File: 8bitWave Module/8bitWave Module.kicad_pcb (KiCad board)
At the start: 2 copper layers, 99.7 x 64.1 mm, 48 parts, among them IC1 0.96_I2C_OLED, IC2 0.91_I2C_OLED, J1 REM, J2 EAR, J3 EXTENSION, M1 Mounting, M2 Mounting, M3 Mounting, M4 Mounting, SW1 UP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

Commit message: Faceplate sketched out
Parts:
- added REF**: logo, icons:logo, F.Cu at (86.4, 103.1)
- moved J3 5.72 mm to (168.3, 95.2)
- moved JP5 5.72 mm to (168.3, 113.0)
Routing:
- net +5V: track 105.4 -> 111.1 mm
- net +3V3: track 45.0 -> 50.7 mm
- net /D2: track 16.4 -> 10.7 mm
- net /D4: track 13.9 -> 8.41 mm
- net /D8: track 6.99 -> 12.0 mm
- net /SCL: track 115.2 -> 119.8 mm
- net /SDA: track 117.7 -> 121.9 mm
- net Net-(IC1-Pad2): track 113.0 -> 112.2 mm
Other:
- board text removed: "8bit Wave"

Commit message: Finishing touches
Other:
- board text added: "AUDIO AMPLIFIER"
- board text added: "Arduino Nano"
- board text added: "BYPASS"
- board text added: "EXTENSION"
- board text added: "GAIN"
- board text added: "I2C PULL-UP (INSTALL IF NEEDED)"
- board text added: "NO_FILTER"
- board text removed: "I2C PULL-UP"
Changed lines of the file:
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@@
     (area 66.04 72.39 172.720001 147.955001)
     (thickness 1.6)
-    (drawings 54)
+    (drawings 60)
     (tracks 481)
     (zones 0)
@@
       (rotate (xyz 0 0 0))
     )
-  )
-  (module i2c_oled:0.91_I2C_OLED (layer F.Cu)
-    (at 102.235 104.775)
-    (fp_text reference IC2 (at 1.905 -0.127 90) (layer F.SilkS)
-      (effects (font (size 1 1) (thickness 0.15)))
-    )
-    (fp_text value 0.91_I2C_OLED (at 15.24 0) (layer F.Fab)
-      (effects (font (size 1 1) (thickness 0.15)))
-    )
-    (fp_line (start 3 3.81) (end 33 3.81) (layer Dwgs.User) (width 0.15))
-    (fp_line (start 33 3.81) (end 33 -3.81) (layer Dwgs.User) (width 0.15))
-    (fp_line (start 33 -3.81) (end 3 -3.81) (layer Dwgs.User) (width 0.15))
-    (fp_line (start 3 0) (end 3 3.81) (layer Dwgs.User) (width 0.15))
-    (fp_line (start 3 0) (end 3 -3.81) (layer Dwgs.User) (width 0.15))
-    (fp_line (start -1.27 6) (end 36.7 6) (layer F.Fab) (width 0.15))
-    (fp_line (start 36.7 6) (end 36.7 -6) (layer F.Fab) (width 0.15))
-    (fp_line (start 36.7 -6) (end -1.27 -6) (layer F.Fab) (width 0.15))
-    (fp_line (start -1.3 0) (end -1.3 6) (layer F.Fab) (width 0.15))
-    (fp_line (start -1.3 0) (end -1.3 -6) (layer F.Fab) (width 0.15))
-    (pad 1 thru_hole rect (at 0 3.81) (size 1.524 1.524) (drill 0.762) (layers *.Cu *.Mask)
-      (net 6 GND))
-    (pad 2 thru_hole circle (at 0 1.27) (size 1.524 1.524) (drill 0.762) (layers *.Cu *.Mask)
-      (net 38 "Net-(IC1-Pad2)"))
-    (pad 3 thru_hole circle (at 0 -1.27) (size 1.524 1.524) (drill 0.762) (layers *.Cu *.Mask)
-      (net 9 /SCL))
-    (pad 4 thru_hole circle (at 0 -3.81) (size 1.524 1.524) (drill 0.762) (layers *.Cu *.Mask)
-      (net 8 /SDA))
   )
   (module Capacitors_THT:C_Disc_D4.7mm_W2.5mm_P5.00mm (layer F.Cu)
@@
       (effects (font (size 1 1) (thickness 0.15)))
     )
-    (fp_text value USER (at -1.905 0.635 360) (layer F.SilkS)
+    (fp_text value USER (at -1.905 0 360) (layer F.SilkS)
       (effects (font (size 0.8 0.8) (thickness 0.1)))
     )
@@
     )
   )
+  (module i2c_oled:0.91_I2C_OLED (layer F.Cu)
+    (at 102.235 104.775)
+    (fp_text reference IC2 (at 1.905 -0.127 90) (layer F.SilkS)
+      (effects (font (size 1 1) (thickness 0.15)))
+    )
+    (fp_text value 0.91_I2C_OLED (at 15.24 0) (layer F.SilkS)
+      (effects (font (size 1 1) (thickness 0.15)))
+    )
+    (fp_line (start 3 3.81) (end 33 3.81) (layer Dwgs.User) (width 0.15))
+    (fp_line (start 33 3.81) (end 33 -3.81) (layer Dwgs.User) (width 0.15))
+    (fp_line (start 33 -3.81) (end 3 -3.81) (layer Dwgs.User) (width 0.15))
+    (fp_line (start 3 0) (end 3 3.81) (layer Dwgs.User) (width 0.15))
+    (fp_line (start 3 0) (end 3 -3.81) (layer Dwgs.User) (width 0.15))
+    (fp_line (start -1.27 6) (end 36.7 6) (layer F.SilkS) (width 0.15))
+    (fp_line (start 36.7 6) (end 36.7 -6) (layer F.SilkS) (width 0.15))
+    (fp_line (start 36.7 -6) (end -1.27 -6) (layer F.SilkS) (width 0.15))
+    (fp_line (start -1.3 0) (end -1.3 6) (layer F.SilkS) (width 0.15))
+    (fp_line (start -1.3 0) (end -1.3 -6) (layer F.SilkS) (width 0.15))
+    (pad 1 thru_hole rect (at 0 3.81) (size 1.524 1.524) (drill 0.762) (layers *.Cu *.Mask)
+      (net 6 GND))
+    (pad 2 thru_hole circle (at 0 1.27) (size 1.524 1.524) (drill 0.762) (layers *.Cu *.Mask)
+      (net 38 "Net-(IC1-Pad2)"))
+    (pad 3 thru_hole circle (at 0 -1.27) (size 1.524 1.524) (drill 0.762) (layers *.Cu *.Mask)
+      (net 9 /SCL))
+    (pad 4 thru_hole circle (at 0 -3.81) (size 1.524 1.524) (drill 0.762) (layers *.Cu *.Mask)
+      (net 8 /SDA))
+  )
+  (gr_text "Arduino Nano" (at 153.67 99.695) (layer B.SilkS)
+    (effects (font (size 0.8 0.8) (thickness 0.1)) (justify mirror))
+  )
+  (gr_text "AUDIO\nAMPLIFIER" (at 104.14 89.535) (layer B.SilkS)
+    (effects (font (size 0.8 0.8) (thickness 0.1)) (justify mirror))
+  )
+  (gr_text EXTENSION (at 165.735 102.87 90) (layer B.SilkS)
+    (effects (font (size 0.8 0.8) (thickness 0.1)) (justify mirror))
+  )
+  (gr_text BYPASS (at 113.665 87.63) (layer B.SilkS)
+    (effects (font (size 0.8 0.8) (thickness 0.1)) (justify mirror))
+  )
+  (gr_text NO_FILTER (at 113.665 82.55) (layer B.SilkS)
+    (effects (font (size 0.8 0.8) (thickness 0.1)) (justify mirror))
+  )
+  (gr_text GAIN (at 106.68 82.55) (layer B.SilkS)
+    (effects (font (size 0.8 0.8) (thickness 0.1)) (justify mirror))
+  )
   (gr_text github.com/tebl (at 84.328 107.696) (layer F.SilkS)
     (effects (font (size 1 1) (thickness 0.1)))
@@
     (effects (font (size 0.8 0.8) (thickness 0.1)) (justify left mirror))
   )
-  (gr_text "I2C\nPULL-UP" (at 147.32 128.27) (layer B.SilkS)
+  (gr_text "I2C\nPULL-UP\n\n(INSTALL IF\nNEEDED)" (at 147.32 128.27) (layer B.SilkS)
     (effects (font (size 0.8 0.8) (thickness 0.1)) (justify mirror))
   )

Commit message: PAM8403
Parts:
- removed IC2: 0.91_I2C_OLED, i2c_oled:0.91_I2C_OLED
- removed JP2: NO_FILTER, Pin_Headers:Pin_Header_Straight_1x02_Pitch2.54mm
- removed JP3: AMPLIFY, Pin_Headers:Pin_Header_Straight_1x03_Pitch2.54mm
- removed RV1: 10k, Potentiometers:Potentiometer_Triwood_RM-065
- added A3: GF1002, gf1002:GF1002_reverse, F.Cu at (97.2, 110.5)
- added D3: 1n4001, Diodes_THT:D_DO-41_SOD81_P10.16mm_Horizontal, F.Cu at (148.0, 131.4)
- added J4: DC IN, Connectors:BARREL_JACK, F.Cu at (156.8, 128.9)
- added J5: LP_FILTER, Pin_Headers:Pin_Header_Straight_2x03_Pitch2.54mm, F.Cu at (134.0, 104.1)
- added J6: SPI, Pin_Headers:Pin_Header_Straight_1x03_Pitch2.54mm, F.Cu at (72.4, 95.2)
- added J7: EAR_SEL, Pin_Headers:Pin_Header_Straight_2x06_Pitch2.54mm, F.Cu at (115.6, 104.1)
- added JP6: PWR_SEL, Pin_Headers:Pin_Header_Straight_1x03_Pitch2.54mm, F.Cu at (151.8, 131.4)
- added REF**: logo, icons:logo, F.Cu at (84.5, 96.9)
- added RV2: 10k, pot_vertical:Potentiometer_Trimmer_Bourns_3296W, F.Cu at (123.8, 88.9)
- C10: value 100uF -> 220uF
- C9: value 10pF -> 47nF
- JP1: footprint Pin_Headers:Pin_Header_Straight_1x02_Pitch2.54mm -> Pin_Headers:Pin_Header_Straight_1x03_Pitch2.54mm
- R5: value 100 -> 10
- R6, R7: value 220 -> 330
- REF**: moved to B.Cu
- moved R5 51.5 mm to (125.7, 112.4), turned to 180 degrees
- moved C9 32.1 mm to (111.7, 104.8), turned to 180 degrees
- moved R7 28.0 mm to (137.8, 123.8), turned to 0 degrees
- moved R6 27.3 mm to (137.8, 127.6), turned to 0 degrees
- moved R8 22.0 mm to (137.8, 108.6), turned to 270 degrees
- moved REF** 18.5 mm to (88.3, 121.5), turned to 180 degrees
- moved R9 17.8 mm to (141.6, 108.6), turned to 270 degrees
- moved C10 16.5 mm to (102.9, 107.3)
- moved C5 8.70 mm to (111.7, 101.0), turned to 180 degrees
- moved C8 8.64 mm to (102.2, 90.2), turned to 180 degrees
- moved JP4 8.13 mm to (108.6, 80.0), turned to 90 degrees
- moved JP1 6.98 mm to (98.4, 80.0)
- moved U1 6.54 mm to (106.0, 89.5)
- moved C7 5.53 mm to (109.9, 85.7), turned to 90 degrees
- moved C6 5.12 mm to (118.1, 94.6), turned to 270 degrees
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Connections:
- A1 pad 30: (no net) -> VIN
- C5 pad 1: +5V -> VEXT
- C6 pad 1: +5V -> VEXT
- C9 pad 1: Net-(C10-Pad2) -> LM386+
- J2 pad 1: GND -> Net-(J2-Pad1)
- J2 pad 5: Net-(J2-Pad5) -> Net-(C10-Pad2)
- R3 pad 1: /SOUND -> Net-(J5-Pad5)
- U1 pad 5: Net-(C10-Pad1) -> LM386+
- U1 pad 6: +5V -> VEXT
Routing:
- net VEXT: track 0.00 -> 80.7 mm, vias 0 -> 6
- net /SOUND: track 108.0 -> 41.0 mm, vias 1 -> 0
- net AUD_LINE: track 0.00 -> 67.0 mm, vias 0 -> 1
- net Net-(J2-Pad1): track 0.00 -> 64.1 mm, vias 0 -> 2
- net /SDA: track 121.9 -> 58.4 mm, vias 2 -> 1
- net /SCK: track 79.8 -> 142.9 mm, vias 2 -> 3
- net /SCL: track 119.8 -> 61.0 mm, vias 4 -> 1
- net /MOSI: track 90.0 -> 148.7 mm, vias 3 -> 5
- net /MISO: track 90.1 -> 143.9 mm
- net GF1002+: track 0.00 -> 39.6 mm
- net GF1002-: track 0.00 -> 37.6 mm
- net Net-(J5-Pad5): track 0.00 -> 28.0 mm, vias 0 -> 1
- net Net-(C10-Pad2): track 31.2 -> 58.4 mm, vias 0 -> 2
- net Net-(D1-Pad2): track 99.7 -> 72.8 mm, vias 0 -> 1
- net Net-(D2-Pad2): track 13.9 -> 39.6 mm
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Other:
- outline, holes or cut-outs redrawn
- net class Power added: clearance 0.381, trace_width 0.381, via_dia 1, via_drill 0.4
- board text added: "(GF1002 module to be installed as alternative amplifier, mounted upside down - adjust to fit under faceplate)"
- board text added: "(PWR_SEL should be set to intended voltage, mark selection for reference. 9V only with LM386 option.)"
- board text added: "5V (DC)"
- board text added: "9V (DC)"
- board text added: "EAR"
- board text added: "EAR_SEL"
- board text added: "EAR_SEL (J7): 01-02 Direct* 11-12 03-04 Direc (AC) 11-12 05-06 LM386 11-12 07-08 GF1002 09-10"
- board text added: "G"
- board text added: "GND"
- board text added: "L"
- board text added: "LM386"
- board text added: "LM386 VOLUME"
- board text added: "LP_FILTER"
- board text added: "LP_FILTER (J6): 1-2 Disabled* 3-4 Enabled 5-6"
- board text added: "R"
- board text added: "REM"
- board text added: "SCL"
- board text added: "SDA"
- board text added: "VCC"
- board text removed: "1-2 Direct 2-3 Amplified"
- board text removed: "AUDIO AMPLIFIER"
- board text removed: "NO_FILTER"

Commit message: Gerber export
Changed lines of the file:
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@@
     (visible_elements 7FFFFFFF)
     (pcbplotparams
-      (layerselection 0x011fc_80000001)
+      (layerselection 0x011fc_ffffffff)
       (usegerberextensions true)
       (usegerberattributes false)
@@
     (descr "LED, diameter 5.0mm, 2 pins, http://cdn-reichelt.de/documents/datenblatt/A500/LL-504BC2E-009.pdf")
     (tags "LED diameter 5.0mm 2 pins")
-    (fp_text reference D2 (at 1.27 -3.96 270) (layer F.SilkS)
-      (effects (font (size 1 1) (thickness 0.15)))
-    )
+    (fp_text reference D2 (at 1.27 0 270) (layer F.SilkS)
+      (effects (font (size 1 1) (thickness 0.15)))
+    )

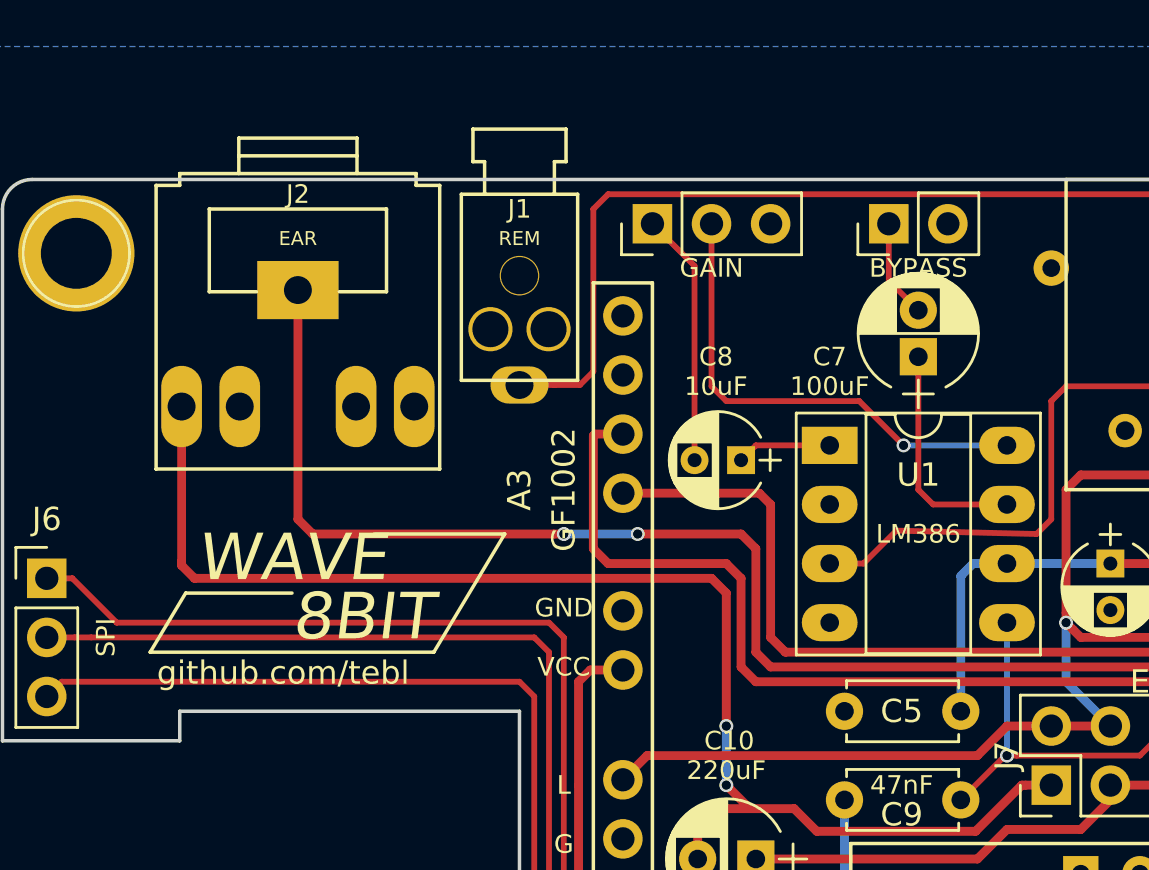
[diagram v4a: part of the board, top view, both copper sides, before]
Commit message: Moved bypass cap, gain jumpers
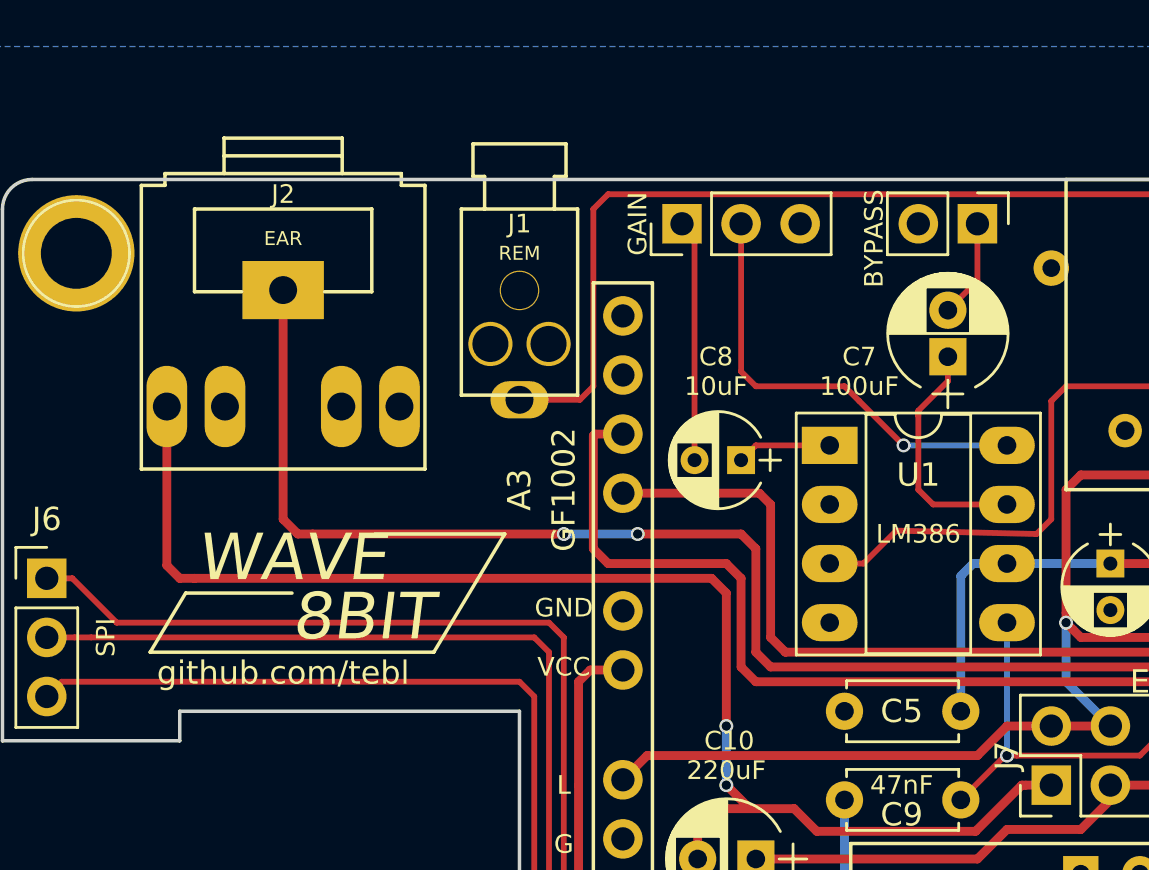
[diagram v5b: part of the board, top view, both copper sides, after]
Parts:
- moved JP4 3.81 mm to (112.4, 80.0), turned to 270 degrees
- moved C7 1.27 mm to (111.1, 85.7)
- moved JP1 1.27 mm to (99.7, 80.0)
- moved J1 0.64 mm to (92.7, 79.4)
- moved J2 0.64 mm to (82.5, 84.5)
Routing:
- net Net-(JP1-Pad2): track 20.7 -> 19.1 mm
- net Net-(J2-Pad1): track 64.1 -> 64.8 mm
- net Net-(C10-Pad2): track 58.4 -> 59.0 mm
- net /REM: track 93.0 -> 93.6 mm
- net Net-(C8-Pad2): track 10.9 -> 10.4 mm
- net Net-(C7-Pad1): track 9.79 -> 10.3 mm

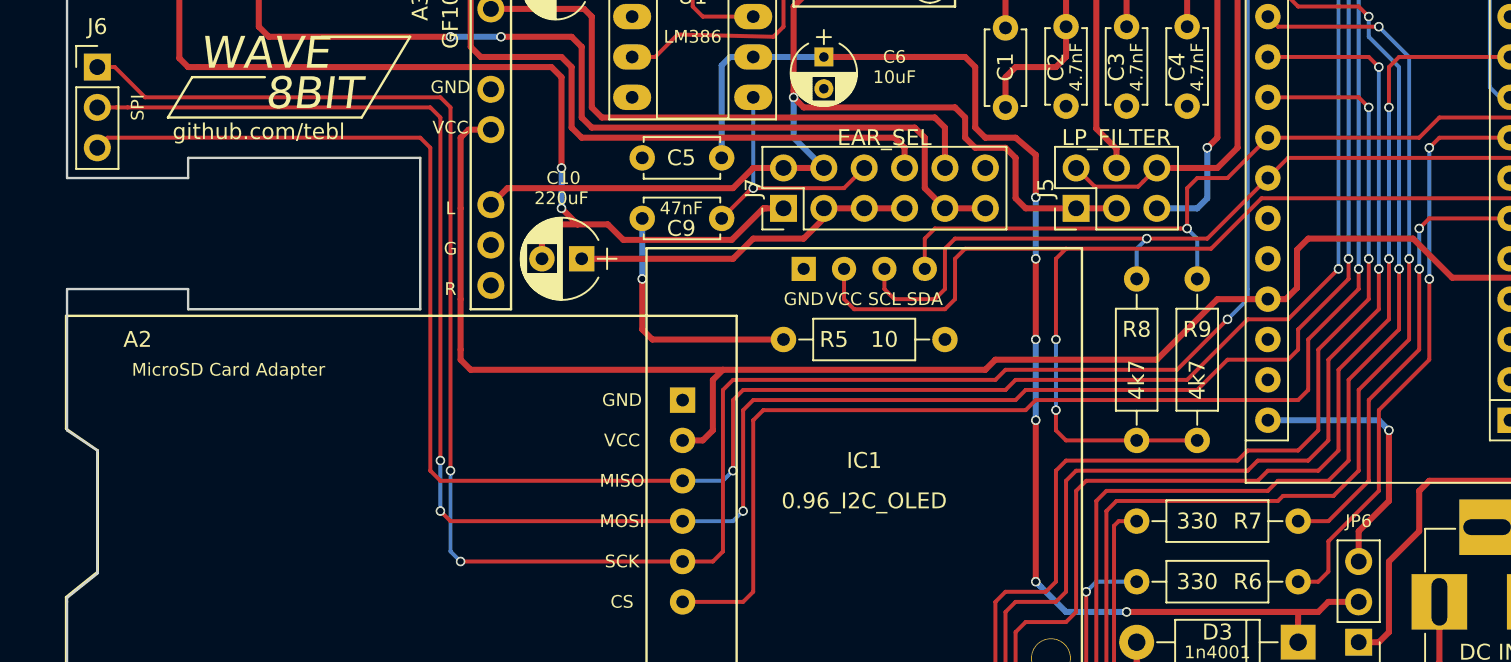
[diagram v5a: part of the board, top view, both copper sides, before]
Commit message: Tweaked module and placement
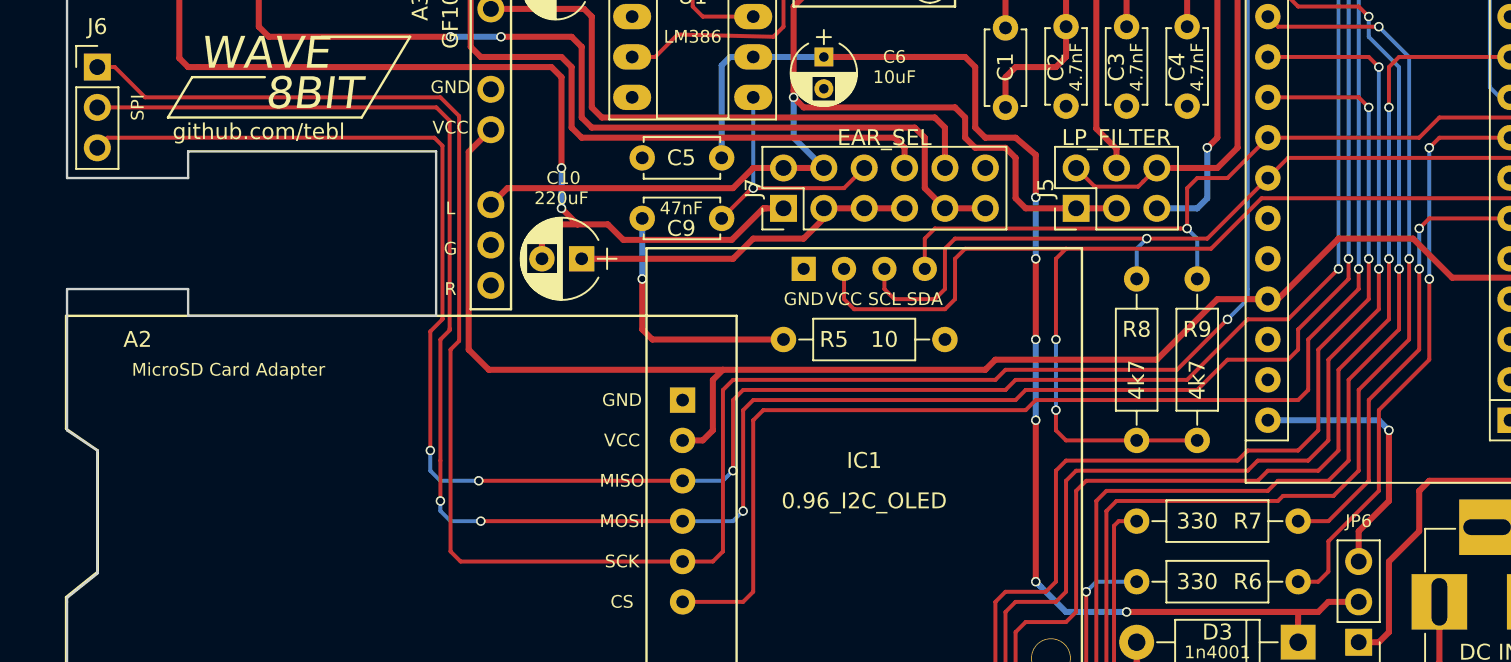
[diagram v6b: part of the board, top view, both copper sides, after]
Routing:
- net +5V: track 133.4 -> 130.1 mm
- net /MISO: track 143.9 -> 145.1 mm, vias 3 -> 5
- net /MOSI: track 148.7 -> 149.3 mm
- net /SCK: track 142.9 -> 143.4 mm, vias 3 -> 1
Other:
- outline, holes or cut-outs redrawn
- board text added: "EAR_SEL (J7): 01-02 Direct* 11-12 03-04 Direct (AC) 11-12 05-06 LM386 11-12 07-08 GF1002 09-10"
- board text added: "LP_FILTER (J5): 1-2 Disabled* 3-4 Enabled 5-6"
- board text added: "Low-pass filter components, set LP_FILTER 1-2 for disable or when not installed"
- board text added: "PWR_SEL"
- board text removed: "EAR_SEL (J7): 01-02 Direct* 11-12 03-04 Direc (AC) 11-12 05-06 LM386 11-12 07-08 GF1002 09-10"
- board text removed: "LP_FILTER (J6): 1-2 Disabled* 3-4 Enabled 5-6"
